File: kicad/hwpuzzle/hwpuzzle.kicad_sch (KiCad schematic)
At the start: 23 parts

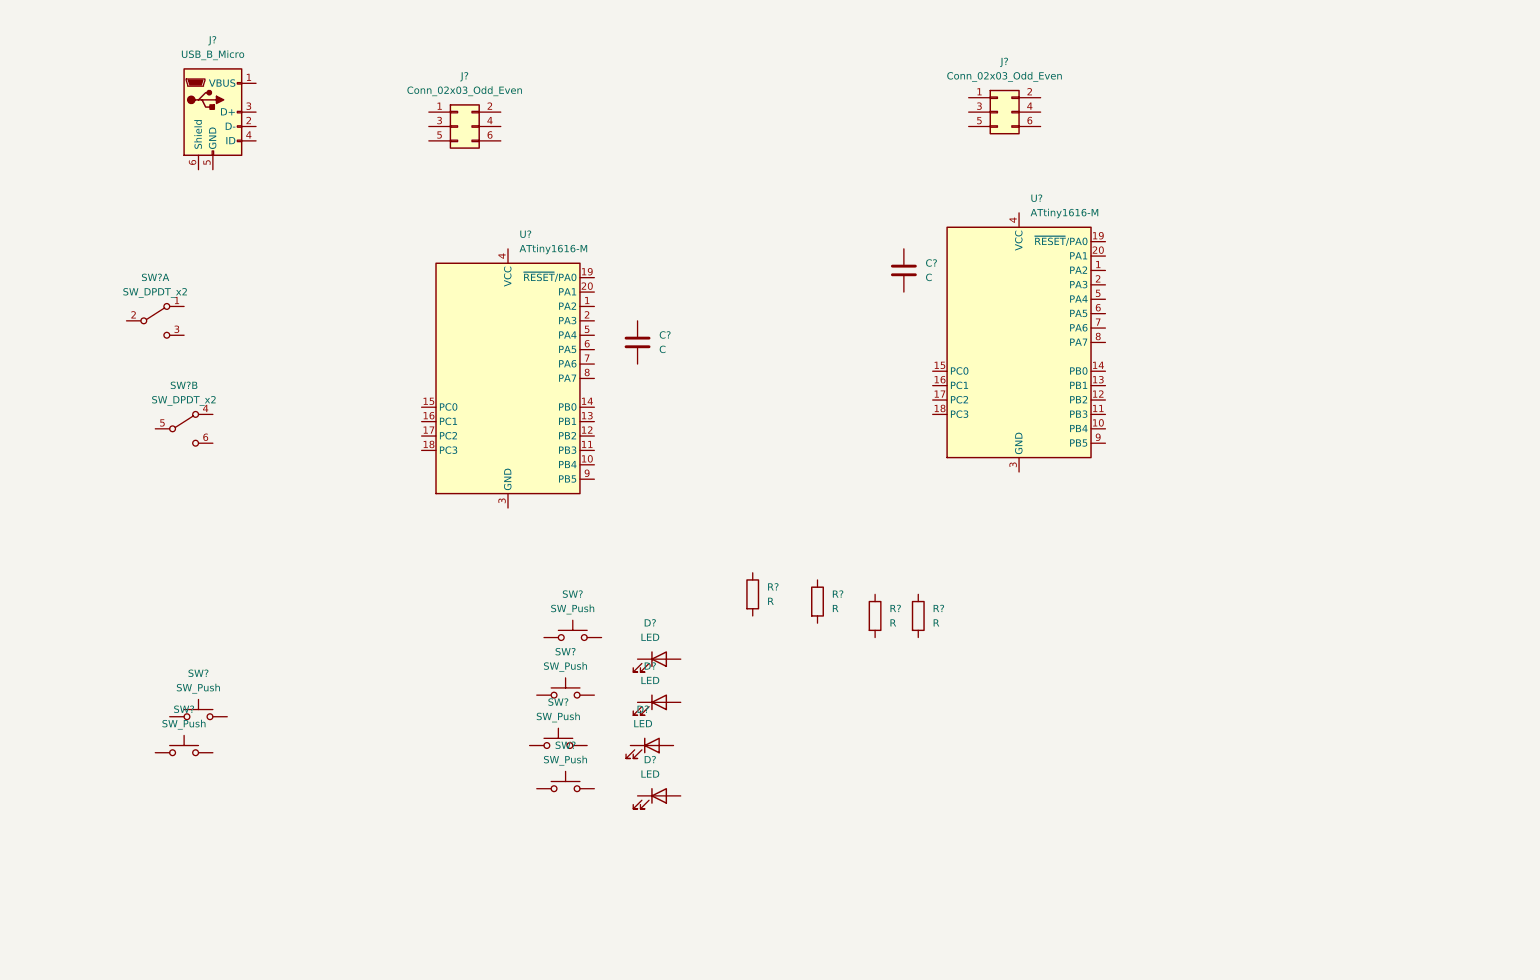
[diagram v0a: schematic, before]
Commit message: Update PCB, add docs
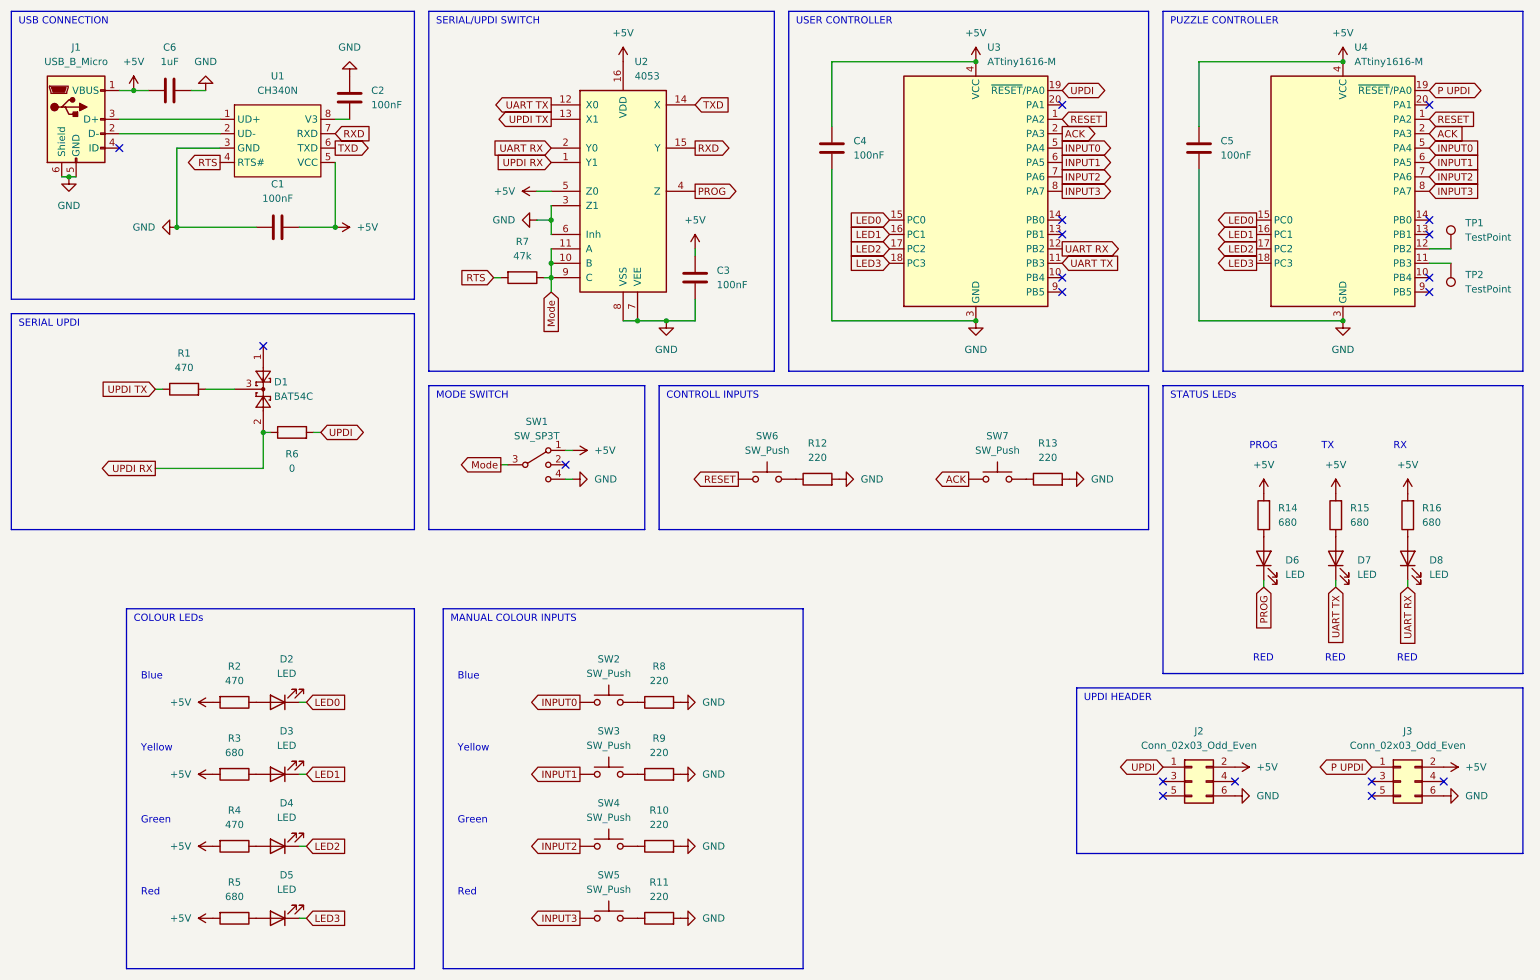
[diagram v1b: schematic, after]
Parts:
- removed D? (x4): LED, symbol Device:LED
- removed R? (x4): R, symbol Device:R
- removed SW? (x2): SW_DPDT_x2, symbol Switch:SW_DPDT_x2
- added C1, C2, C3: 100nF, Capacitor_SMD:C_0402_1005Metric, symbol Device:C
- added C6: 1uF, Capacitor_SMD:C_0402_1005Metric, symbol Device:C
- added D1: BAT54C, Package_TO_SOT_SMD:SOT-23, symbol Diode:BAT54C
- added D2, D3, D4, D5, D6, D7, D8: LED, LED_SMD:LED_0603_1608Metric, symbol Device:LED
- added R1, R2, R4: 470, Resistor_SMD:R_0402_1005Metric, symbol Device:R
- added R10, R11, R12, R13, R8, R9: 220, Resistor_SMD:R_0402_1005Metric, symbol Device:R
- added R14, R15, R16, R3, R5: 680, Resistor_SMD:R_0402_1005Metric, symbol Device:R
- added R6: 0, Resistor_SMD:R_0402_1005Metric, symbol Device:R
- added R7: 47k, Resistor_SMD:R_0402_1005Metric, symbol Device:R
- added SW1: SW_SP3T, Button_Switch_SMD:SW_SP3T_PCM13, symbol Switch:SW_SP3T
- added TP1, TP2: TestPoint, TestPoint:TestPoint_Pad_D1.0mm, symbol Connector:TestPoint
- added U1: CH340N, Package_SO:SOP-8_3.9x4.9mm_P1.27mm, symbol hwpuzzle:CH340N
- added U2: 4053, Package_SO:TSSOP-16_4.4x5mm_P0.65mm, symbol 4xxx:4053
- C4, C5: renamed from C?; value C -> 100nF; footprint (none) -> Capacitor_SMD:C_0402_1005Metric; LCSC (none) -> C1525; MPN (none) -> CL05B104KO5NNNC
- J1: renamed from J?; footprint (none) -> hwpuzzle:MicroXNJ; LCSC (none) -> C404969; MPN (none) -> MicroXNJ
- J2, J3: renamed from J?; footprint (none) -> Connector_PinHeader_2.54mm:PinHeader_2x03_P2.54mm_Vertical; LCSC (none) -> DNP; MPN (none) -> DNP
- SW2, SW3, SW4, SW5, SW6, SW7: renamed from SW?; footprint (none) -> Button_Switch_SMD:SW_SPST_TL3342; LCSC (none) -> C318884; MPN (none) -> TS-1187A-B-A-B
- U3, U4: renamed from U?; LCSC (none) -> C507118; MPN (none) -> ATTINY1616-MNR
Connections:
- net +5V: now reaches C4.1
- net +5V: now also C5.1, J1.1 (VBUS), J2.2 (Pin_2), J3.2 (Pin_2), U3.4 (VCC), U4.4 (VCC), C1.2, C3.1, C6.1, R14.2, R15.2, R16.2, R2.2, R3.2, R4.2, R5.2, SW1.1, U1.5 (VCC), U2.16 (VDD), U2.5 (Z0)
- net GND: now reaches C4.2
- net GND: now also C5.2, J1.5 (GND), J1.6 (Shield), J2.6 (Pin_6), J3.6 (Pin_6), U3.21 (GND), U3.3 (GND), U4.21 (GND), U4.3 (GND), C1.1, C2.1, C3.2, C6.2, R10.2, R11.2, R12.2, R13.2, R8.2, R9.2, SW1.4, U1.3 (GND), U2.3 (Z1), U2.6 (Inh), U2.7 (VEE), U2.8 (VSS)
- net INPUT1: now reaches SW3.1
- net INPUT1: now also U3.6 (PA5), U4.6 (PA5)
- net at SW3.2: now also R9.1
- net P UPDI: now reaches J3.1 (Pin_1)
- net P UPDI: now also U4.19 (~{RESET}/PA0)
- net INPUT2: now reaches SW4.1
- net INPUT2: now also U3.7 (PA6), U4.7 (PA6)
- net at SW4.2: now also R10.1
- net RESET: now reaches U3.1 (PA2)
- net RESET: now also SW6.1, U4.1 (PA2)
- net UART TX: now reaches U3.11 (PB3)
- net UART TX: now also D7.1 (K), U2.12 (X0)
- net UART RX: now reaches U3.12 (PB2)
- net UART RX: now also D8.1 (K), U2.2 (Y0)
- net LED0: now reaches U3.15 (PC0)
- net LED0: now also U4.15 (PC0), D2.1 (K)
- net LED1: now reaches U3.16 (PC1)
- net LED1: now also U4.16 (PC1), D3.1 (K)
- net LED2: now reaches U3.17 (PC2)
- net LED2: now also U4.17 (PC2), D4.1 (K)
- net LED3: now reaches U3.18 (PC3)
- net LED3: now also U4.18 (PC3), D5.1 (K)
- net UPDI: now reaches U3.19 (~{RESET}/PA0)
- net UPDI: now also J2.1 (Pin_1), R6.2
- net ACK: now reaches U3.2 (PA3)
- net ACK: now also SW7.1, U4.2 (PA3)
- net INPUT0: now reaches U3.5 (PA4)
- net INPUT0: now also SW2.1, U4.5 (PA4)
- net INPUT3: now reaches U3.8 (PA7)
- net INPUT3: now also SW5.1, U4.8 (PA7)
- net at SW7.2: now also R13.1
- net at SW5.2: now also R11.1
- net at SW2.2: now also R8.1
- net at SW6.2: now also R12.1
- net at J1.2 (D-): now also U1.2 (UD-)
- net at J1.3 (D+): now also U1.1 (UD+)
- net at U4.11 (PB3): now also TP2.1
- net at U4.12 (PB2): now also TP1.1
- new net: D1.3, R1.2
- new net: D4.2 (A), R4.1
- new net: D6.2 (A), R14.1
- new net: D5.2 (A), R5.1
- new net: D3.2 (A), R3.1
- new net: D8.2 (A), R16.1
- new net: C2.2, U1.8 (V3)
- new net: D2.2 (A), R2.1
- new net: D7.2 (A), R15.1
- new net Mode: R7.1, SW1.3, U2.10 (B), U2.11 (A), U2.9 (C)
- new net PROG: D6.1 (K), U2.4 (Z)
- new net RTS: R7.2, U1.4 (RTS#)
- new net RXD: U1.7 (RXD), U2.15 (Y)
- new net TXD: U1.6 (TXD), U2.14 (X)
- new net UPDI RX: D1.2, R6.1, U2.1 (Y1)
- new net UPDI TX: R1.1, U2.13 (X1)
- no-connect marks 0 -> 19
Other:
- note added: "Blue"
- note added: "COLOUR LEDs"
- note added: "CONTROLL INPUTS"
- note added: "Green"
- note added: "MANUAL COLOUR INPUTS"
- note added: "MODE SWITCH"
- note added: "PROG"
- note added: "PUZZLE CONTROLLER"
- note added: "RED"
- note added: "RX"
- note added: "Red"
- note added: "SERIAL UPDI"
- note added: "SERIAL/UPDI SWITCH"
- note added: "STATUS LEDs"
- note added: "TX"
- note added: "UPDI HEADER"
- note added: "USB CONNECTION"
- note added: "USER CONTROLLER"
- note added: "Yellow"
- company: (none) -> buckket.org
- title: (none) -> hwpuzzle
- moved on the sheet: C4, C5, J1, J2, J3, SW2, SW3, SW4, SW5, SW6, SW7, U3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
